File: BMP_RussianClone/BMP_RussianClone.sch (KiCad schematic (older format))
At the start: 57 parts, among them J1 BARREL_JACK, Q1 MMBT3904, Q2 MMBT3904, Q3 MMBT3904, Q4 MMBT3904

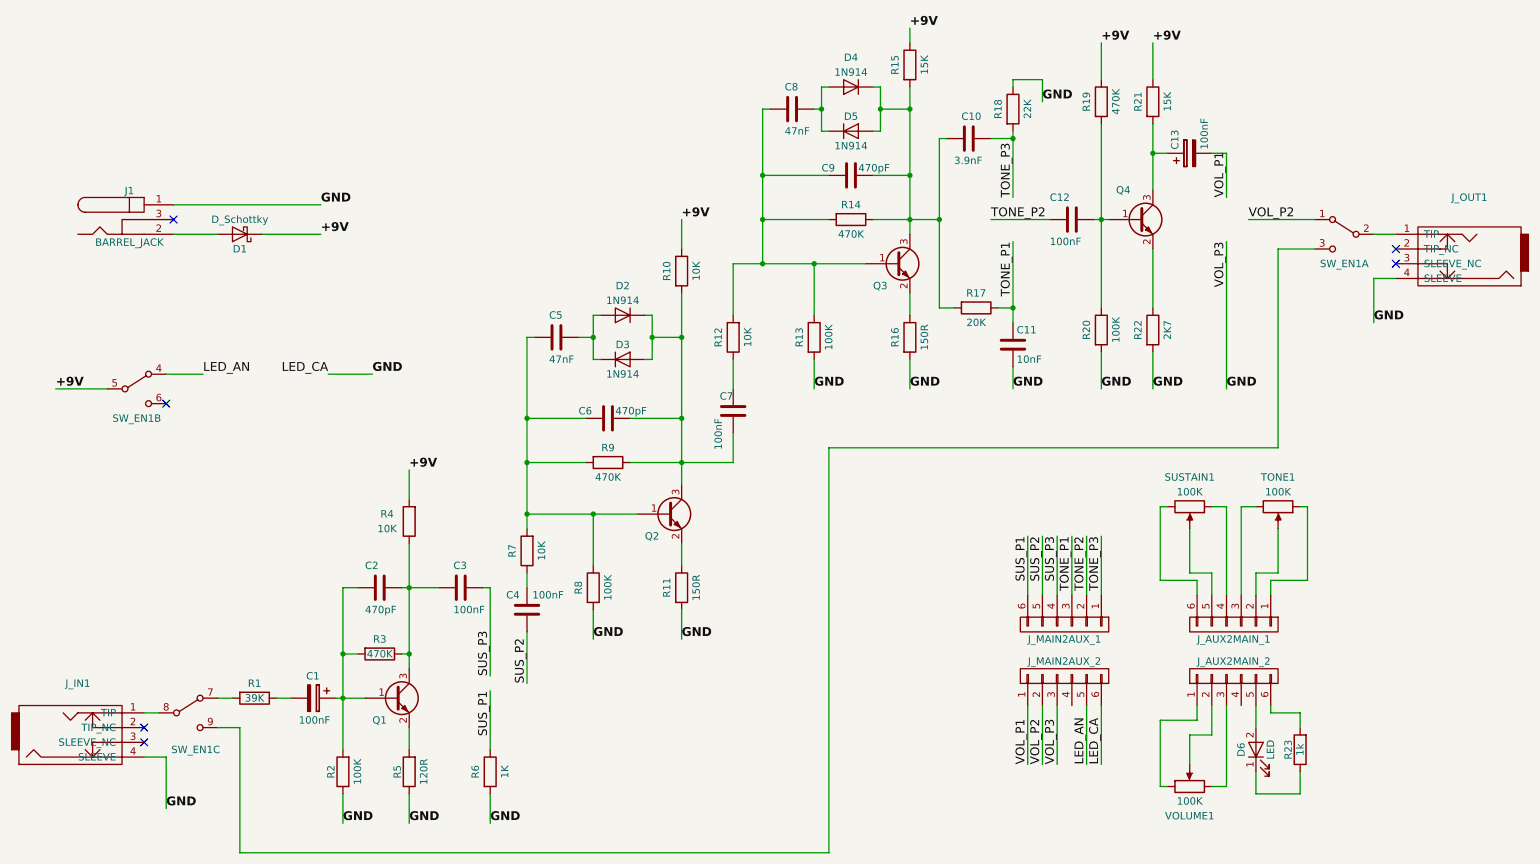
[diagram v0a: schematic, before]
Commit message: Added SuperCollider Schema and Layout
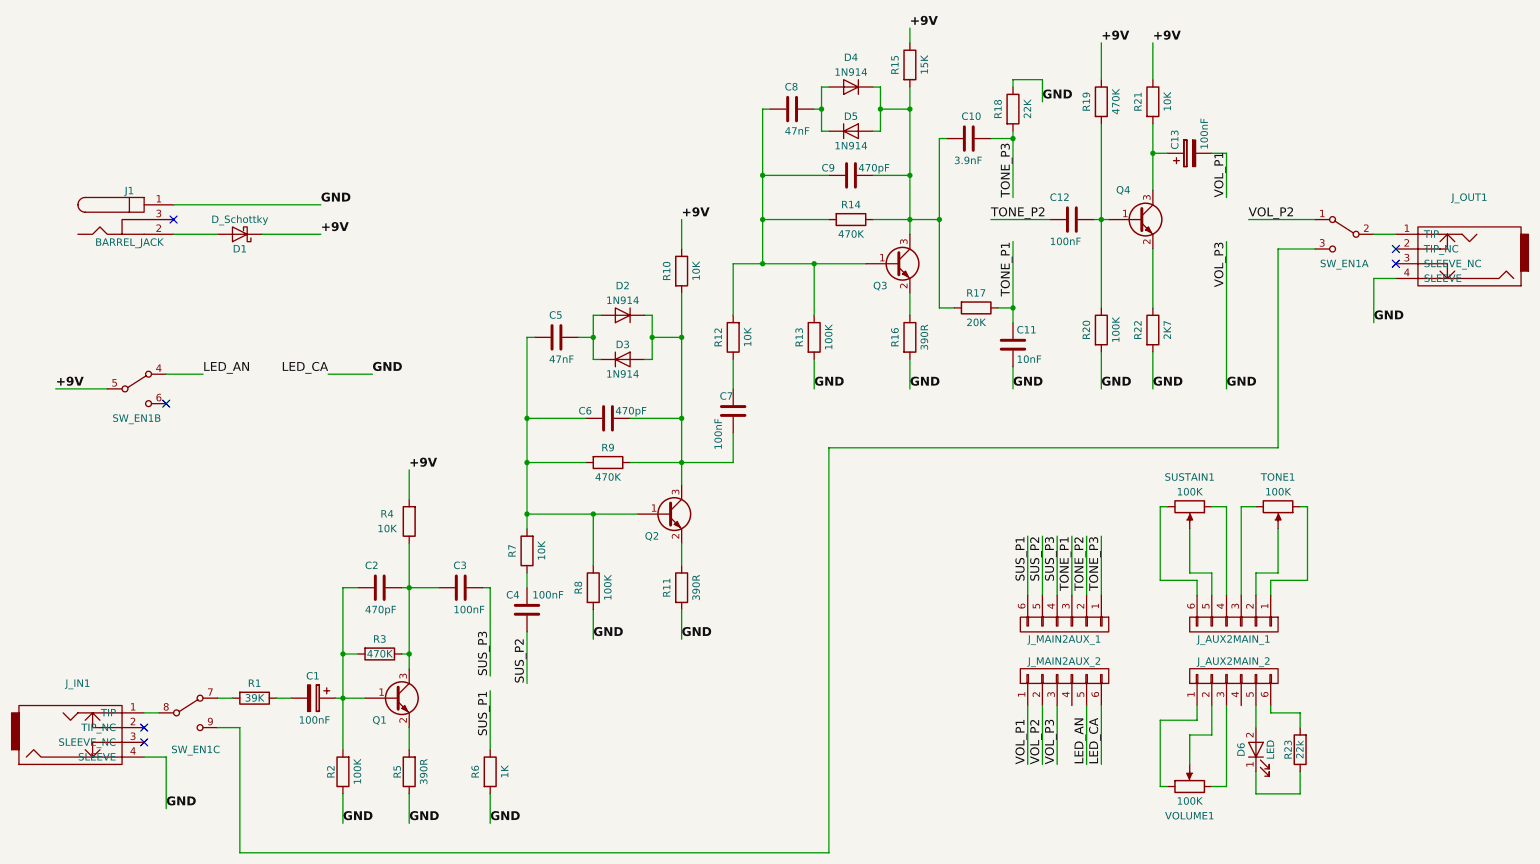
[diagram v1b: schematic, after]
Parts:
- R11, R16: value 150R -> 390R
- R21: value 15K -> 10K
- R23: value 1k -> 22k
- R5: value 120R -> 390R
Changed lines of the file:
@@
 P 3450 6000
 F 0 "R5" V 3530 6000 50  0000 C CNN
-F 1 "120R" V 3350 6000 50  0000 C CNN
+F 1 "390R" V 3350 6000 50  0000 C CNN
 F 2 "Resistors_SMD:R_0805_HandSoldering" V 3380 6000 50  0001 C CNN
 F 3 "" H 3450 6000 50  0001 C CNN
@@
 P 5300 4750
 F 0 "R11" V 5200 4750 50  0000 C CNN
-F 1 "150R" V 5400 4750 50  0000 C CNN
+F 1 "390R" V 5400 4750 50  0000 C CNN
 F 2 "Resistors_SMD:R_0805_HandSoldering" V 5230 4750 50  0001 C CNN
 F 3 "" H 5300 4750 50  0001 C CNN
@@
 P 6850 3050
 F 0 "R16" V 6750 3050 50  0000 C CNN
-F 1 "150R" V 6950 3050 50  0000 C CNN
+F 1 "390R" V 6950 3050 50  0000 C CNN
 F 2 "Resistors_SMD:R_0805_HandSoldering" V 6780 3050 50  0001 C CNN
 F 3 "" H 6850 3050 50  0001 C CNN
@@
 P 8500 1450
 F 0 "R21" V 8400 1450 50  0000 C CNN
-F 1 "15K" V 8600 1450 50  0000 C CNN
+F 1 "10K" V 8600 1450 50  0000 C CNN
 F 2 "Resistors_SMD:R_0805_HandSoldering" V 8430 1450 50  0001 C CNN
 F 3 "" H 8500 1450 50  0001 C CNN
@@
 P 9500 5850
 F 0 "R23" V 9580 5850 50  0000 C CNN
-F 1 "1k" V 9500 5850 50  0000 C CNN
+F 1 "22k" V 9500 5850 50  0000 C CNN
 F 2 "Resistors_SMD:R_0805_HandSoldering" V 9430 5850 50  0001 C CNN
 F 3 "" H 9500 5850 50  0001 C CNN
